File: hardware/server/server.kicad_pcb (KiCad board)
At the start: 2 copper layers, 43.2 x 51.4 mm, 12 parts

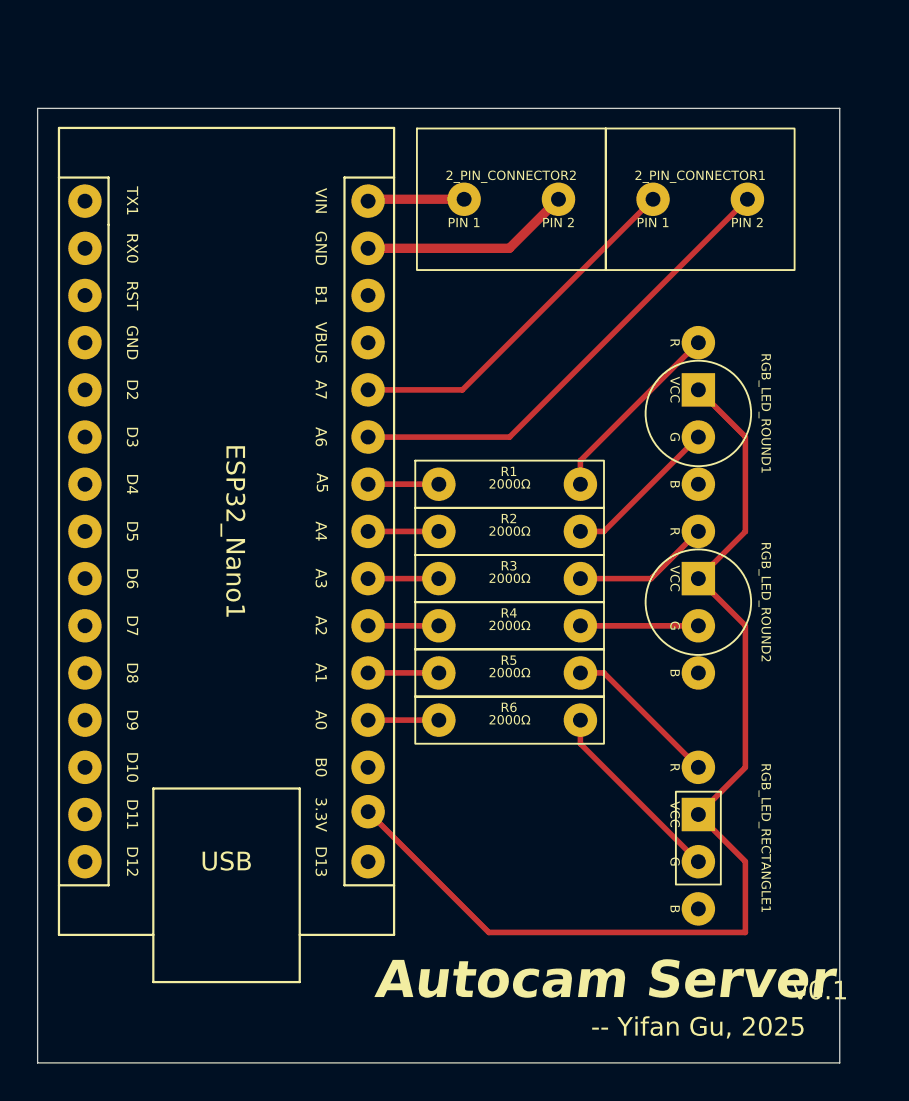
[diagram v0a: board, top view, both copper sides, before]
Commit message: hardware/tag: Add Autocam Tag PCB.
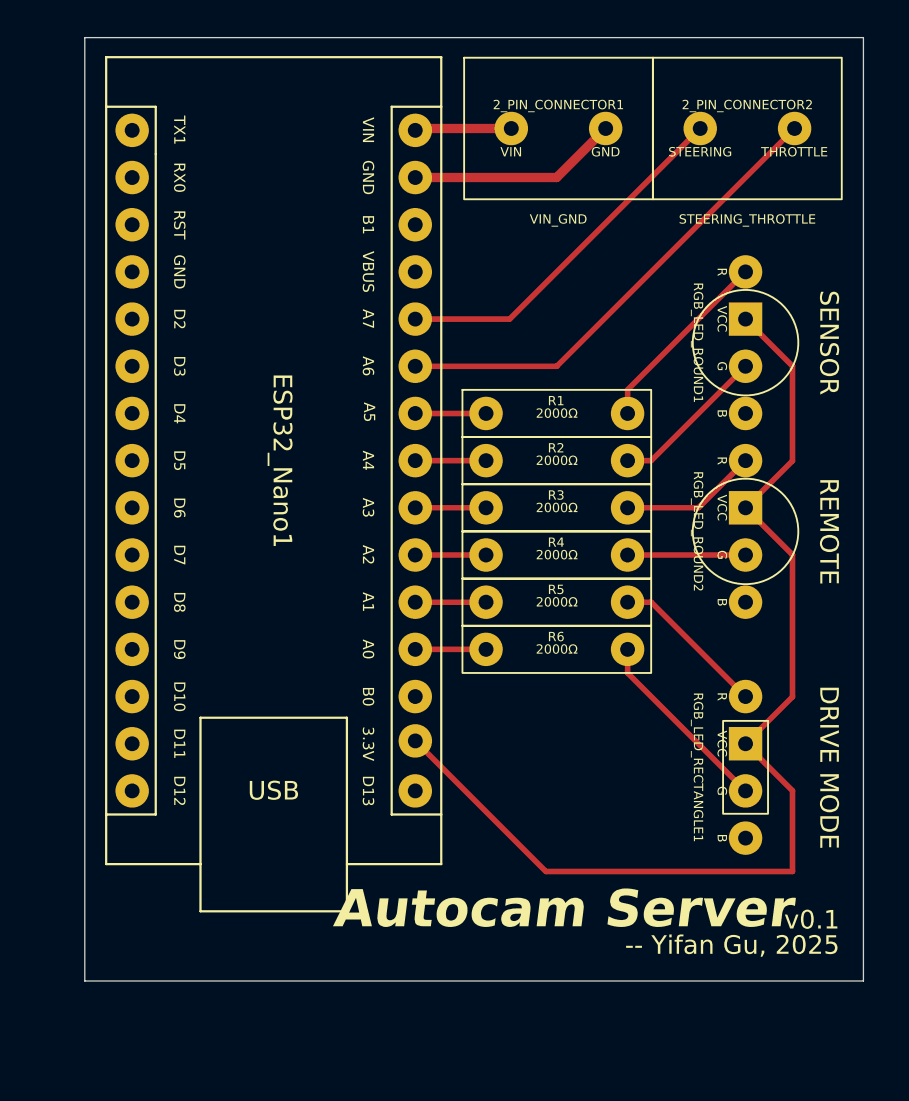
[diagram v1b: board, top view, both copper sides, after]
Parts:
- RGB_LED_RECTANGLE1: value DRIVE_MODE_LED -> DRIVE MODE
- RGB_LED_ROUND1: value SENSOR_STATE_LED -> SENSOR
- RGB_LED_ROUND2: value REMOTE_STATE_LED -> REMOTE
- moved R2 4.58 mm to (153.7, 91.4)
- moved R3 4.58 mm to (153.7, 94.0)
- moved R4 4.58 mm to (153.7, 96.5)
- moved R5 4.58 mm to (153.7, 99.1)
- moved R6 4.58 mm to (153.7, 101.6)
- moved R1 4.58 mm to (153.7, 88.9)
- moved 2_PIN_CONNECTOR1 4.58 mm to (152.5, 77.4)
- moved 2_PIN_CONNECTOR2 4.58 mm to (162.7, 77.4)
- moved ESP32_Nano1 4.58 mm to (134.6, 73.7)
- moved RGB_LED_RECTANGLE1 4.58 mm to (167.7, 108.0)
- moved RGB_LED_ROUND1 4.58 mm to (167.7, 85.1)
- moved RGB_LED_ROUND2 4.58 mm to (167.7, 95.2)
- renumbered 2_PIN_CONNECTOR2 to 2_PIN_CONNECTOR1, 2_PIN_CONNECTOR1 to 2_PIN_CONNECTOR2
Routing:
- net Net-(ESP32_Nano1-3.3V): track 57.4 -> 58.2 mm
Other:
- board size 43.2 x 51.4 mm -> 41.9 x 50.8 mm

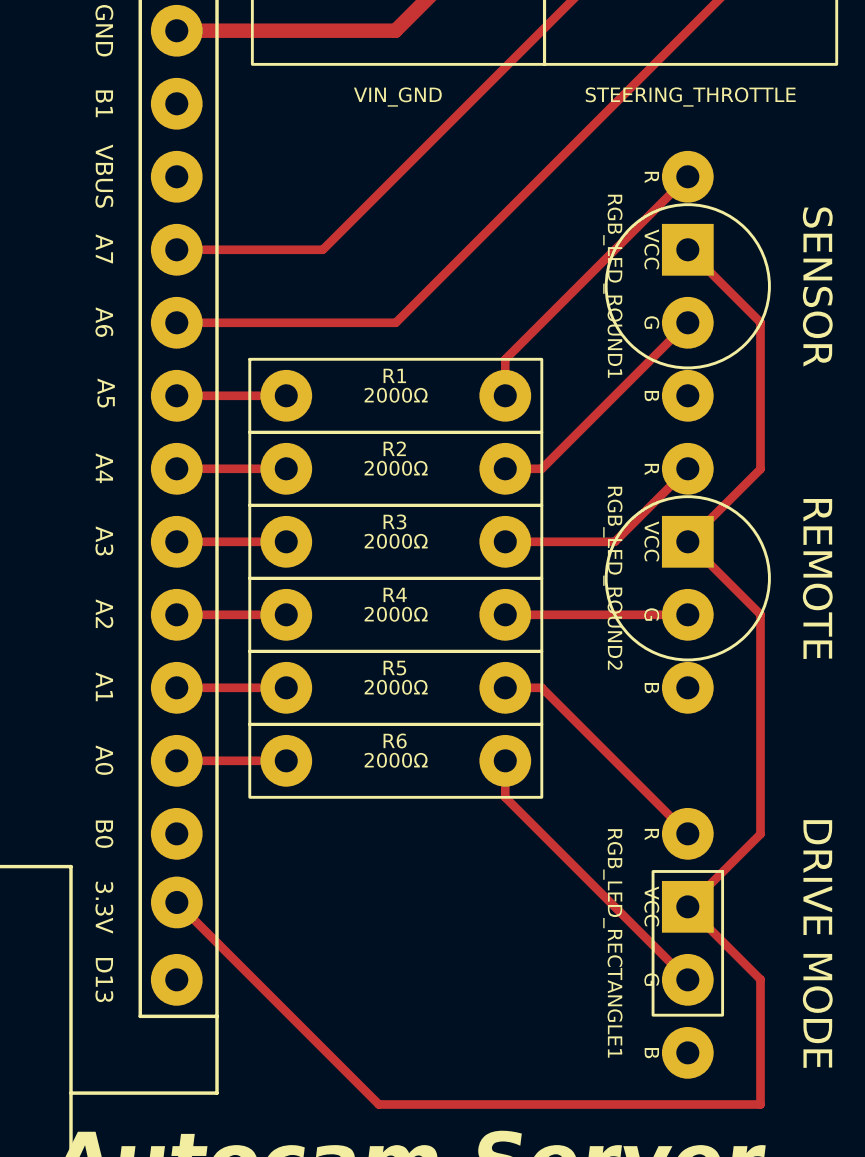
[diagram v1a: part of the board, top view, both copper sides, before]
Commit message: hardware: Add more footprint measurement.
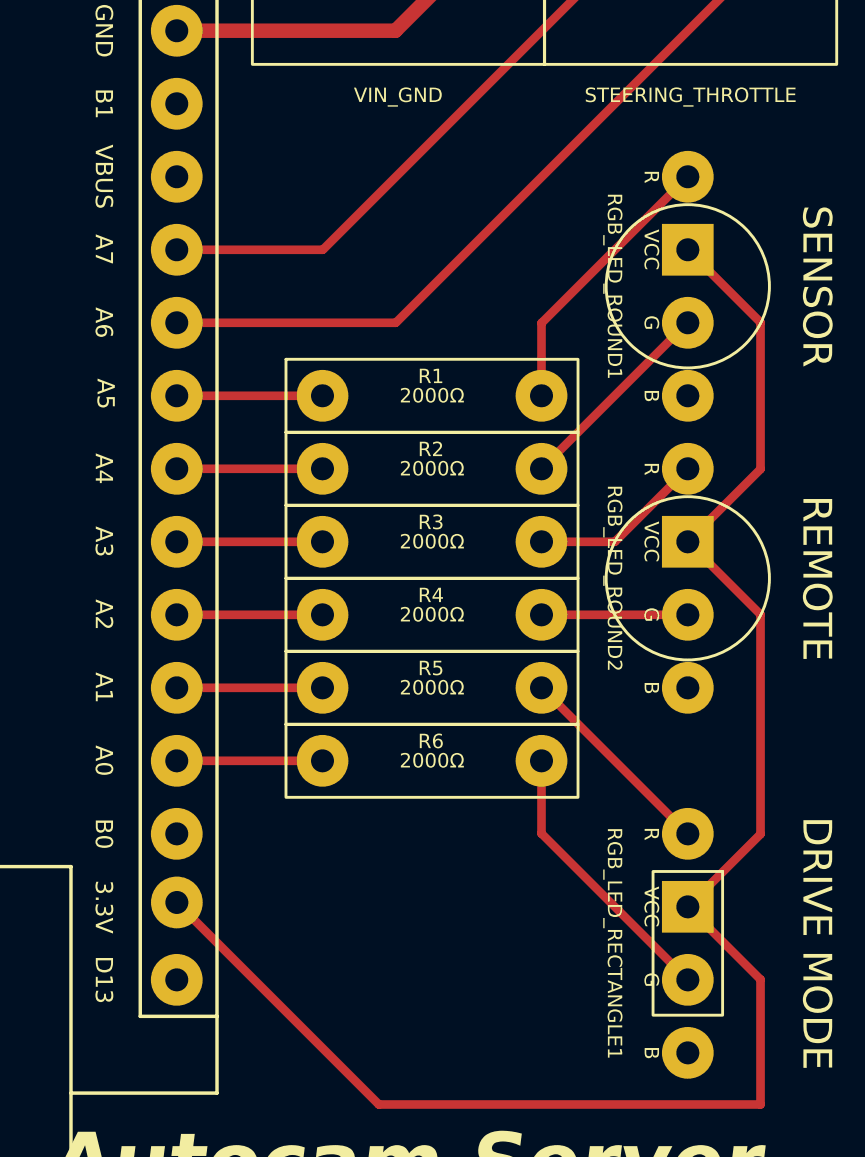
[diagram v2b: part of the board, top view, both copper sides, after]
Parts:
- moved R1 1.26 mm to (154.9, 88.9)
- moved R2 1.26 mm to (154.9, 91.4)
- moved R3 1.26 mm to (154.9, 94.0)
- moved R4 1.26 mm to (154.9, 96.5)
- moved R5 1.26 mm to (154.9, 99.1)
- moved R6 1.26 mm to (154.9, 101.6)
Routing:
- net Net-(RGB_LED_ROUND2-R): track 7.40 -> 6.14 mm
- net Net-(RGB_LED_ROUND2-G): track 6.35 -> 5.09 mm
- net Net-(RGB_LED_RECTANGLE1-R): track 8.45 -> 7.19 mm
- net Net-(ESP32_Nano1-A5): track 3.81 -> 5.07 mm
- net Net-(ESP32_Nano1-A4): track 3.81 -> 5.07 mm
- net Net-(ESP32_Nano1-A3): track 3.81 -> 5.07 mm
- net Net-(ESP32_Nano1-A2): track 3.81 -> 5.07 mm
- net Net-(ESP32_Nano1-A1): track 3.81 -> 5.07 mm
- net Net-(ESP32_Nano1-A0): track 3.81 -> 5.07 mm
- net Net-(RGB_LED_ROUND1-G): track 8.45 -> 7.19 mm
- net Net-(RGB_LED_ROUND1-R): track 10.3 -> 9.73 mm
- net Net-(RGB_LED_RECTANGLE1-G): track 10.3 -> 9.73 mm

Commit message: hardware: Add remote PCB.
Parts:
- moved R1 1.27 mm to (153.7, 88.9)
- moved R2 1.27 mm to (153.7, 91.4)
- moved R3 1.27 mm to (153.7, 94.0)
- moved R4 1.27 mm to (153.7, 96.5)
- moved R5 1.27 mm to (153.7, 99.1)
- moved R6 1.27 mm to (153.7, 101.6)
- moved RGB_LED_RECTANGLE1 1.27 mm to (166.4, 108.0)
- moved RGB_LED_ROUND1 1.27 mm to (166.4, 85.1)
- moved RGB_LED_ROUND2 1.27 mm to (166.4, 95.2)
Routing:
- net Net-(ESP32_Nano1-3.3V): track 58.2 -> 56.4 mm
- net Net-(ESP32_Nano1-A5): track 5.07 -> 3.80 mm
- net Net-(ESP32_Nano1-A4): track 5.07 -> 3.80 mm
- net Net-(ESP32_Nano1-A3): track 5.07 -> 3.80 mm
- net Net-(ESP32_Nano1-A2): track 5.07 -> 3.80 mm
- net Net-(ESP32_Nano1-A1): track 5.07 -> 3.80 mm
- net Net-(ESP32_Nano1-A0): track 5.07 -> 3.80 mm
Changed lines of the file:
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@@
 	(footprint "Autocam:Anode RGB LED (Round)"
 		(layer "F.Cu")
-		(at 167.65 95.25 -90)
+		(at 166.38 95.25 -90)
 		(property "Reference" "RGB_LED_ROUND2"
 			(at 0 2.55 270)
@@
 	(footprint "Autocam:Simple Resistor"
 		(layer "F.Cu")
-		(at 154.94 88.9)
+		(at 153.67 88.9)
 		(property "Reference" "R1"
 			(at 3.774036 -0.672769 0)
@@
 	(footprint "Autocam:Simple Resistor"
 		(layer "F.Cu")
-		(at 154.94 93.98)
+		(at 153.67 93.98)
 		(property "Reference" "R3"
 			(at 3.774036 -0.672769 0)
@@
 	(footprint "Autocam:Simple Resistor"
 		(layer "F.Cu")
-		(at 154.94 91.44)
+		(at 153.67 91.44)
 		(property "Reference" "R2"
 			(at 3.774036 -0.672769 0)
@@
 	(footprint "Autocam:Anode RGB LED (Rectangle)"
 		(layer "F.Cu")
-		(at 167.65 107.95 -90)
+		(at 166.38 107.95 -90)
 		(property "Reference" "RGB_LED_RECTANGLE1"
 			(at 0 2.55 270)
@@
 	(footprint "Autocam:Anode RGB LED (Round)"
 		(layer "F.Cu")
-		(at 167.65 85.09 -90)
+		(at 166.38 85.09 -90)
 		(property "Reference" "RGB_LED_ROUND1"
 			(at 0 2.55 270)
@@
 	(footprint "Autocam:Simple Resistor"
 		(layer "F.Cu")
-		(at 154.94 99.06)
+		(at 153.67 99.06)
 		(property "Reference" "R5"
 			(at 3.774036 -0.672769 0)
@@
 	(footprint "Autocam:Simple Resistor"
 		(layer "F.Cu")
-		(at 154.94 101.6)
+		(at 153.67 101.6)
 		(property "Reference" "R6"
 			(at 3.774036 -0.672769 0)
@@
 	(footprint "Autocam:Simple Resistor"
 		(layer "F.Cu")
-		(at 154.94 96.52)
+		(at 153.67 96.52)
 		(property "Reference" "R4"
 			(at 3.774036 -0.672769 0)
@@
 	)
 	(segment
-		(start 170.29 73.56)
-		(end 157.49 86.36)
+		(start 157.49 86.36)
+		(end 170.29 73.56)
 		(width 0.3)
 		(layer "F.Cu")
@@
 	)
 	(segment
-		(start 157.49 86.36)
-		(end 149.87 86.36)
+		(start 149.87 86.36)
+		(end 157.49 86.36)
 		(width 0.3)
 		(layer "F.Cu")
@@
 	(segment
 		(start 149.87 88.9)
-		(end 154.94 88.9)
+		(end 153.67 88.9)
 		(width 0.3)
 		(layer "F.Cu")
@@
 	(segment
 		(start 149.87 96.52)
-		(end 154.94 96.52)
+		(end 153.67 96.52)
 		(width 0.3)
 		(layer "F.Cu")
@@
 	(segment
 		(start 149.87 99.06)
-		(end 154.94 99.06)
+		(end 153.67 99.06)
 		(width 0.3)
 		(layer "F.Cu")
@@
 	(segment
 		(start 149.87 91.44)
-		(end 154.94 91.44)
+		(end 153.67 91.44)
 		(width 0.3)
 		(layer "F.Cu")
@@
 	)
 	(segment
-		(start 167.65 81.28)
-		(end 162.56 86.37)
+		(start 166.38 81.28)
+		(end 161.29 86.37)
 		(width 0.3)
 		(layer "F.Cu")
@@
 	)
 	(segment
-		(start 162.56 86.37)
-		(end 162.56 88.9)
+		(start 161.29 86.37)
+		(end 161.29 88.9)
 		(width 0.3)
 		(layer "F.Cu")
@@
 	)
 	(segment
-		(start 167.64 86.36)
-		(end 162.56 91.44)
+		(start 166.37 86.36)
+		(end 161.29 91.44)
 		(width 0.3)
 		(layer "F.Cu")
@@
 	)
 	(segment
-		(start 167.65 86.36)
-		(end 167.64 86.36)
+		(start 166.38 86.36)
+		(end 166.37 86.36)
 		(width 0.3)
 		(layer "F.Cu")
@@
 	)
 	(segment
-		(start 167.65 91.44)
-		(end 165.11 93.98)
+		(start 166.38 91.44)
+		(end 163.84 93.98)
 		(width 0.3)
 		(layer "F.Cu")
@@
 	)
 	(segment
-		(start 165.11 93.98)
-		(end 162.56 93.98)
+		(start 163.84 93.98)
+		(end 161.29 93.98)
 		(width 0.3)
 		(layer "F.Cu")
@@
 	)
 	(segment
-		(start 167.65 96.52)
-		(end 162.56 96.52)
+		(start 166.38 96.52)
+		(end 161.29 96.52)
 		(width 0.3)
 		(layer "F.Cu")
@@
 	)
 	(segment
-		(start 162.57 99.06)
-		(end 162.56 99.06)
+		(start 161.3 99.06)
+		(end 161.29 99.06)
 		(width 0.3)
 		(layer "F.Cu")
@@
 	)
 	(segment
-		(start 167.65 104.14)
-		(end 162.57 99.06)
+		(start 166.38 104.14)
+		(end 161.3 99.06)
 		(width 0.3)
 		(layer "F.Cu")
@@
 	)
 	(segment
-		(start 162.56 104.13)
-		(end 162.56 101.6)
+		(start 161.29 104.13)
+		(end 161.29 101.6)
 		(width 0.3)
 		(layer "F.Cu")
@@
 	)
 	(segment
-		(start 167.65 109.22)
-		(end 162.56 104.13)
+		(start 166.38 109.22)
+		(end 161.29 104.13)
 		(width 0.3)
 		(layer "F.Cu")
@@
 	(segment
 		(start 149.87 93.98)
-		(end 154.94 93.98)
+		(end 153.67 93.98)
 		(width 0.3)
 		(layer "F.Cu")
@@
 	(segment
 		(start 149.87 101.6)
-		(end 154.94 101.6)
+		(end 153.67 101.6)
 		(width 0.3)
 		(layer "F.Cu")
@@
 	)
 	(segment
-		(start 167.65 93.98)
-		(end 170.18 96.51)
+		(start 166.38 93.98)
+		(end 168.91 96.51)
 		(width 0.3)
 		(layer "F.Cu")
@@
 	)
 	(segment
-		(start 167.65 106.68)
-		(end 170.18 109.21)
+		(start 168.91 104.15)
+		(end 166.38 106.68)
 		(width 0.3)
 		(layer "F.Cu")
@@
 	)
 	(segment
-		(start 170.18 104.15)
-		(end 167.65 106.68)
+		(start 166.53537 114.13463)
+		(end 157.48 114.13463)
 		(width 0.3)
 		(layer "F.Cu")
@@
 	)
 	(segment
-		(start 170.18 91.45)
-		(end 167.65 93.98)
+		(start 168.91 109.21)
+		(end 168.91 111.76)
 		(width 0.3)
 		(layer "F.Cu")
@@
 	)
 	(segment
-		(start 170.18 96.51)
-		(end 170.18 104.15)
+		(start 168.91 91.45)
+		(end 166.38 93.98)
 		(width 0.3)
 		(layer "F.Cu")
@@
 	)
 	(segment
-		(start 170.18 113.556935)
-		(end 156.902305 113.556935)
+		(start 168.91 111.76)
+		(end 166.53537 114.13463)
 		(width 0.3)
 		(layer "F.Cu")
@@
 	)
 	(segment
-		(start 170.18 109.21)
-		(end 170.18 113.556935)
+		(start 168.91 96.51)
+		(end 168.91 104.15)
 		(width 0.3)
 		(layer "F.Cu")
@@
 	)
 	(segment
-		(start 156.902305 113.556935)
+		(start 157.48 114.13463)
 		(end 149.873472 106.528102)
 		(width 0.3)
@@
 	)
 	(segment
-		(start 170.18 86.35)
-		(end 170.18 91.45)
+		(start 166.38 106.68)
+		(end 168.91 109.21)
+		(width 0.3)
+		(layer "F.Cu")
+		(net 39)
+	)
+	(segment
+		(start 168.91 86.35)
+		(end 168.91 91.45)
 		(width 0.3)
 		(layer "F.Cu")
@@
 	)
 	(segment
-		(start 167.65 83.82)
-		(end 170.18 86.35)
+		(start 166.38 83.82)
+		(end 168.91 86.35)
 		(width 0.3)
 		(layer "F.Cu")

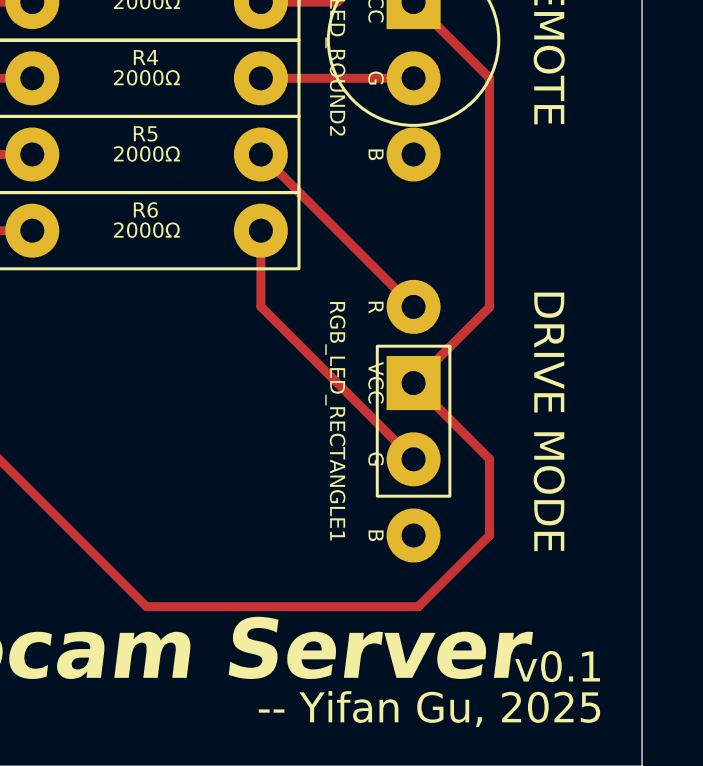
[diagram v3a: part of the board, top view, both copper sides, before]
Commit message: hardware/server: Update LED shape, change to all round LEDs.
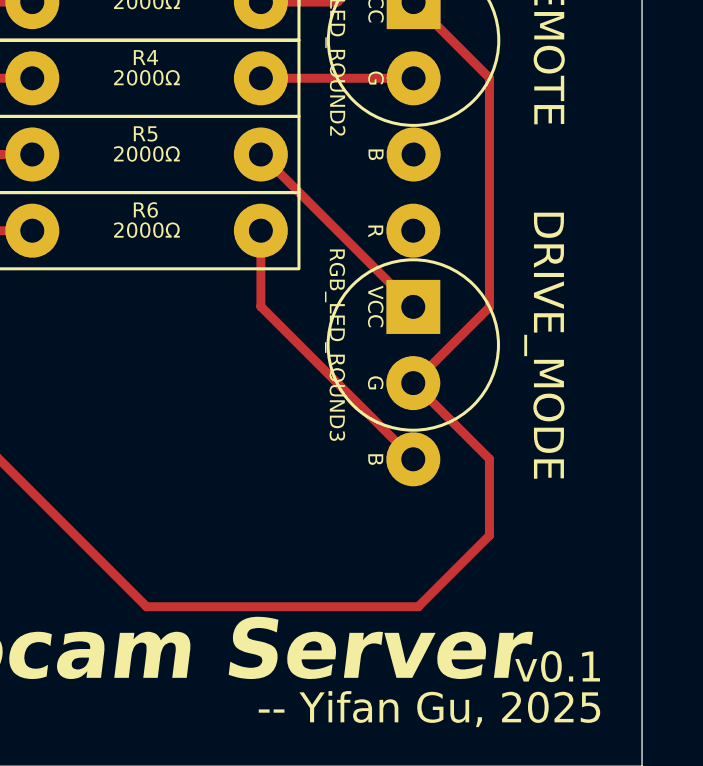
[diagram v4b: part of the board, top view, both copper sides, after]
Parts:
- removed RGB_LED_RECTANGLE1: DRIVE MODE, Autocam:Anode RGB LED (Rectangle)
- added RGB_LED_ROUND3: DRIVE_MODE, Autocam:Anode RGB LED (Round), F.Cu at (166.4, 105.4)

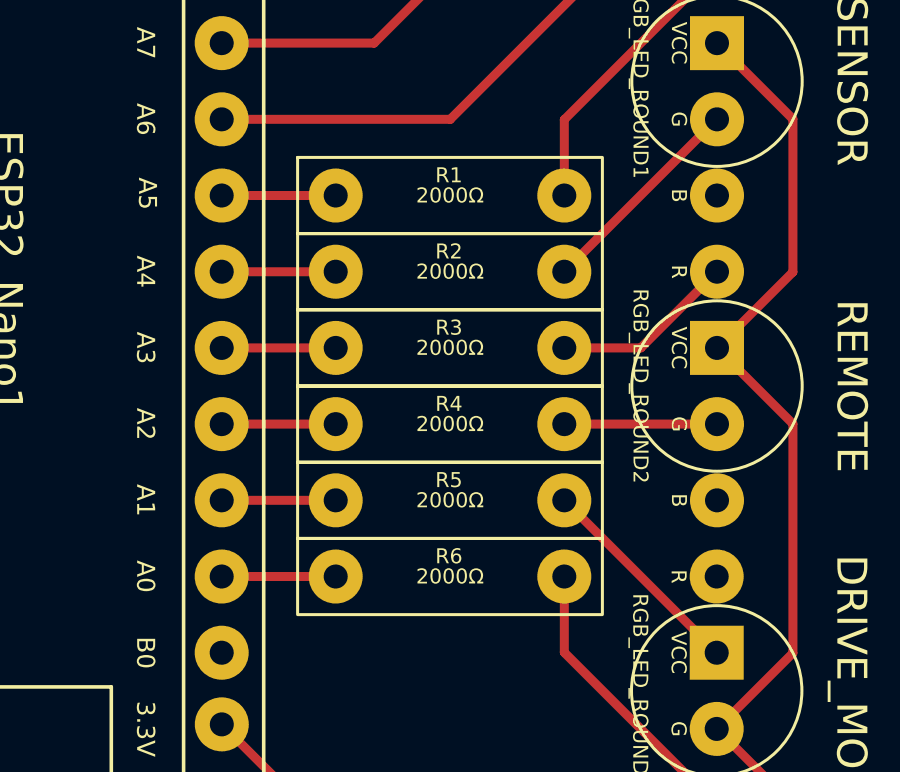
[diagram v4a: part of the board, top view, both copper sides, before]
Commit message: hardware: Increase the LED resistor from 2000Ω to 10KΩ.
To reduce the power consumption.
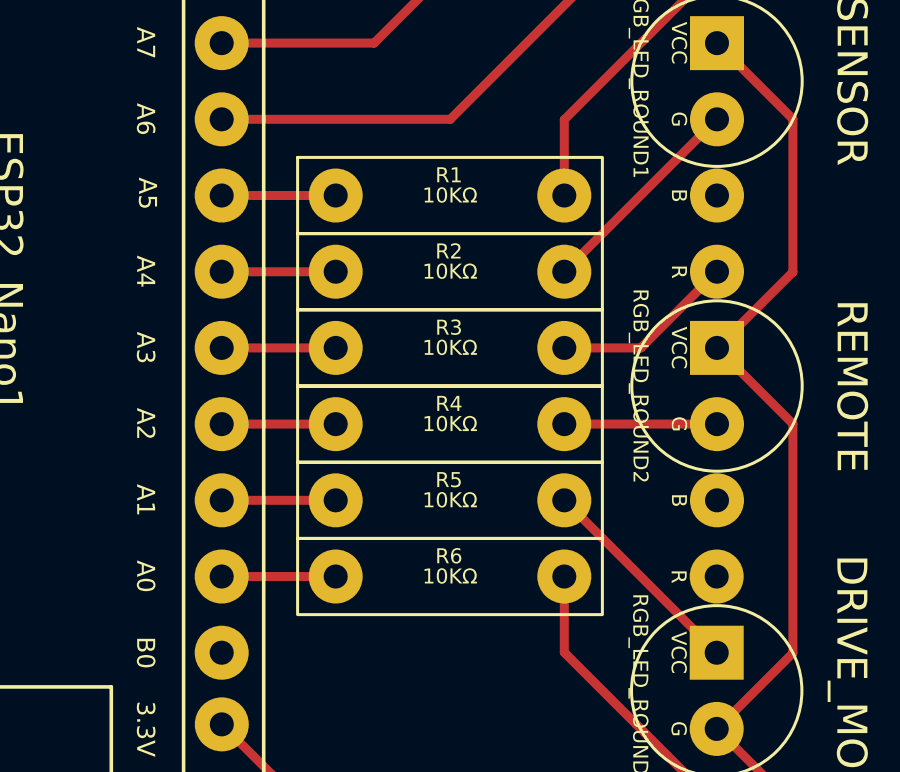
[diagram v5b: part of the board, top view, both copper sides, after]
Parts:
- R1, R2, R3, R4, R5, R6: value 2000Ω -> 10KΩ
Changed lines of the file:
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@@
 			)
 		)
-		(property "Value" "2000Ω"
+		(property "Value" "10KΩ"
 			(at 3.81 0 0)
 			(unlocked yes)
@@
 			)
 		)
-		(property "Value" "2000Ω"
+		(property "Value" "10KΩ"
 			(at 3.81 0 0)
 			(unlocked yes)
@@
 			)
 		)
-		(property "Value" "2000Ω"
+		(property "Value" "10KΩ"
 			(at 3.81 0 0)
 			(unlocked yes)
@@
 			)
 		)
-		(property "Value" "2000Ω"
+		(property "Value" "10KΩ"
 			(at 3.81 0 0)
 			(unlocked yes)
@@
 			)
 		)
-		(property "Value" "2000Ω"
+		(property "Value" "10KΩ"
 			(at 3.81 0 0)
 			(unlocked yes)
@@
 			)
 		)
-		(property "Value" "2000Ω"
+		(property "Value" "10KΩ"
 			(at 3.81 0 0)
 			(unlocked yes)
